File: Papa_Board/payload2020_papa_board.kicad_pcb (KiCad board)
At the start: 4 copper layers, 82 x 82 mm, 88 parts, among them J1 Conn_01x02_Female, J10 Conn_01x02_Female, J2 Conn_01x05, J3 Conn_01x05_Female, J4 Conn_01x05, J5 M80-5000642, J6 M80-5000642, J7 Conn_01x02_Female, J8 693072010801, J9 Conn_01x02_Female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

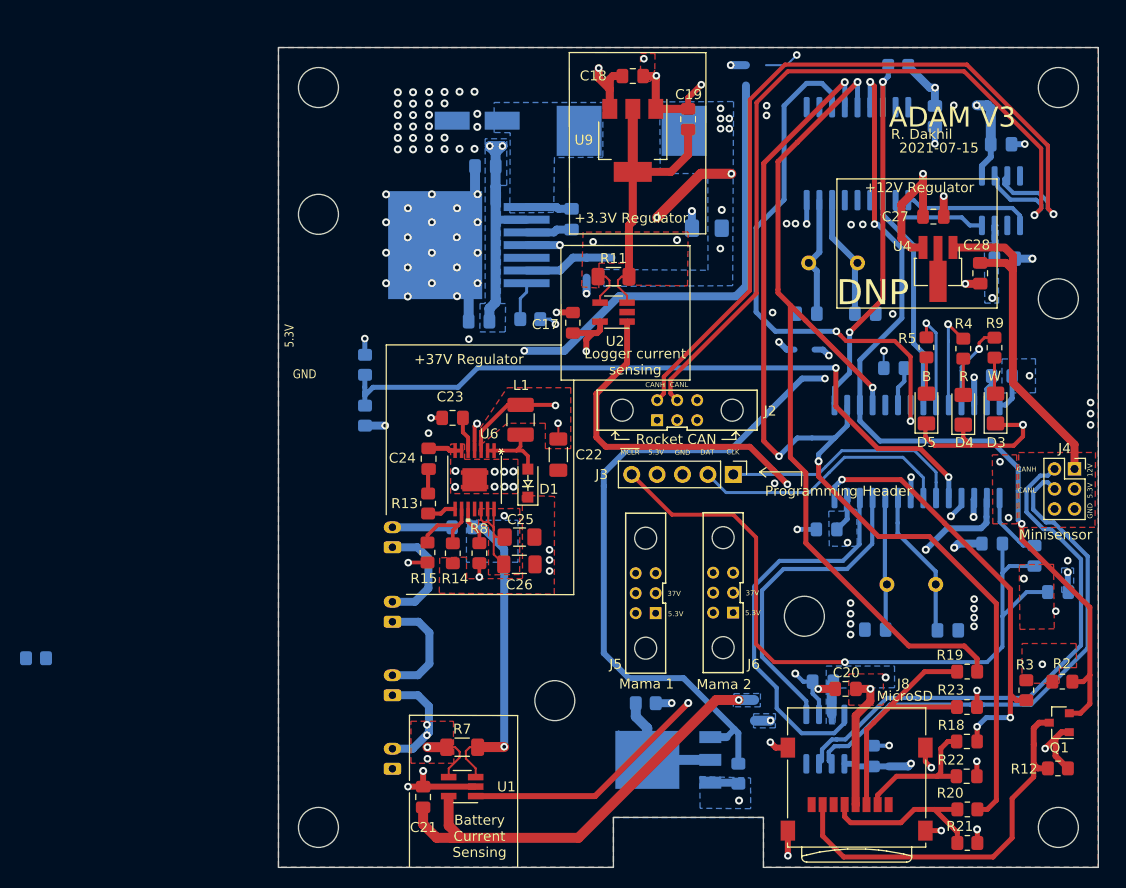
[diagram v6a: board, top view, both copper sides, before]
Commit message: Finish changes to PCB layout, clean up and simplify VCC layer
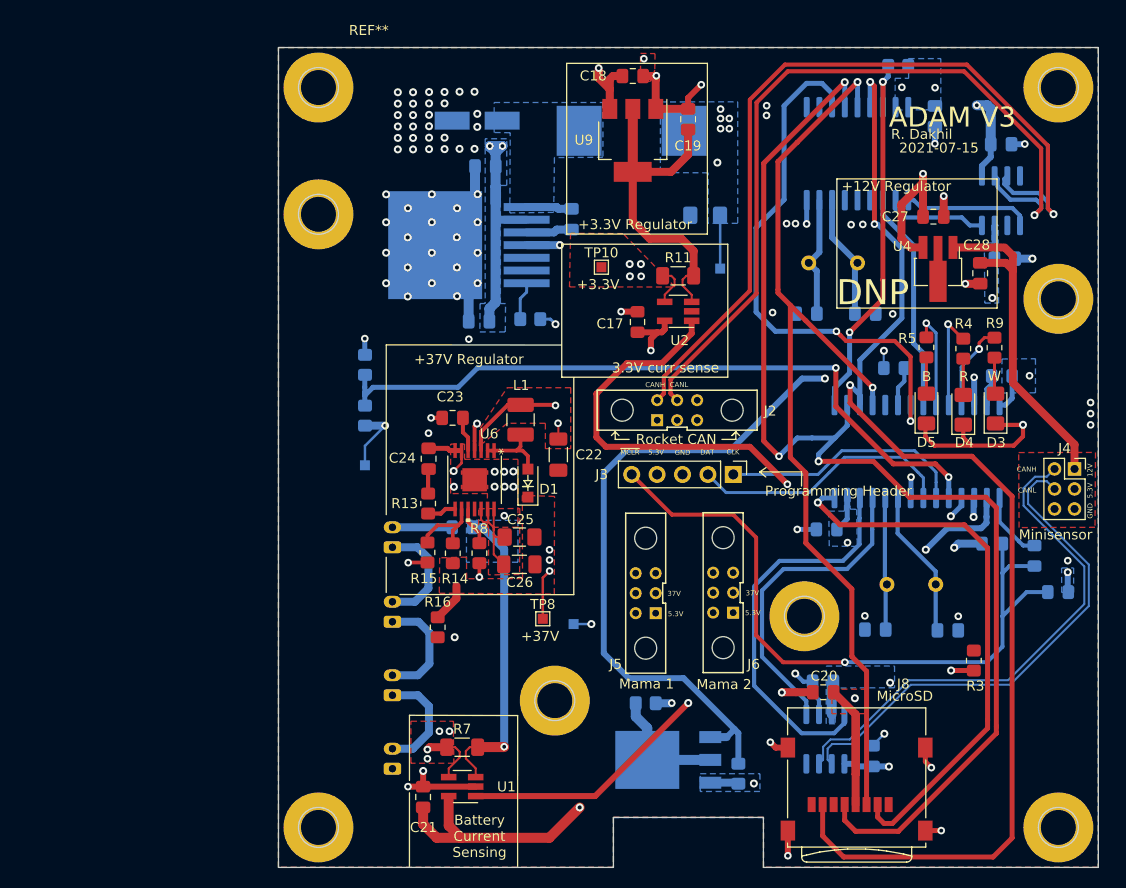
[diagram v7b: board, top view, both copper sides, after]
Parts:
- removed Q1: BSS138, Package_TO_SOT_SMD:SOT-23
- removed R12, R2: 10kR, Resistor_SMD:R_0805_2012Metric_Pad1.20x1.40mm_HandSolder
- removed R18: 68kR, Resistor_SMD:R_0805_2012Metric_Pad1.15x1.40mm_HandSolder
- removed R19, R20: 68kR, Resistor_SMD:R_0805_2012Metric_Pad1.20x1.40mm_HandSolder
- removed R21, R23: 132kR, Resistor_SMD:R_0805_2012Metric_Pad1.20x1.40mm_HandSolder
- removed R22: 132kR, Resistor_SMD:R_0805_2012Metric_Pad1.15x1.40mm_HandSolder
- added ?: , , F.Cu at (93.1, 83.8)
- added ?: , , F.Cu at (92.2, 149.0)
- added ?: , , F.Cu at (189.9, 144.5)
- added ?: , , F.Cu at (192.2, 123.9)
- added ?: , , F.Cu at (129.5, 133.1)
- added ?: , , F.Cu at (190.0, 70.3)
- added ?: , , F.Cu at (191.4, 93.3)
- added REF**: MountingHole_3.5mm_Pad, MountingHole:MountingHole_3.5mm_Pad, F.Cu at (110.9, 70.6)
- added TP10: TestPoint, TestPoint:TestPoint_Pad_1.0x1.0mm, F.Cu at (134.2, 89.8)
- added TP2: TestPoint, TestPoint:TestPoint_Pad_1.0x1.0mm, B.Cu at (131.4, 125.5)
- added TP3: TestPoint, TestPoint:TestPoint_Pad_1.0x1.0mm, B.Cu at (110.5, 109.6)
- added TP6: TestPoint, TestPoint:TestPoint_Pad_1.0x1.0mm, B.Cu at (146.0, 89.9)
- added TP8: TestPoint, TestPoint:TestPoint_Pad_1.0x1.0mm, F.Cu at (128.3, 125.0)
- R16: moved to F.Cu
- moved R16 40.3 mm to (117.8, 125.8), turned to -90 degrees
- moved C17 6.47 mm to (137.8, 95.3)
- moved R11 6.47 mm to (141.8, 90.6)
- moved U2 6.47 mm to (141.8, 94.2)
- moved R3 6.03 mm to (171.4, 129.1), turned to 90 degrees
- moved C20 2.25 mm to (156.3, 132.3)
- moved C7 1.30 mm to (144.5, 84.6)
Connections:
- net /+ renamed /CANH_PAYLOAD
- net /- renamed /CANL_PAYLOAD
- C21 pad 2: +5.3V -> +5V
- C25 pad 1: Net-(C25-Pad1) -> +37V
- C26 pad 1: Net-(C25-Pad1) -> +37V
- D1 pad 1: Net-(C25-Pad1) -> +37V
- J5 pad 2: Net-(J5-Pad2) -> +37V
- J6 pad 2: Net-(J6-Pad2) -> +37V
- J8 pad 2: Net-(J8-Pad2) -> /MCU and CAN controllers/CS_2
- J8 pad 3: Net-(J8-Pad3) -> /MCU and CAN controllers/MOSI
- J8 pad 5: Net-(J8-Pad5) -> /MCU and CAN controllers/SCK
- J8 pad 7: Net-(J8-Pad7) -> /MCU and CAN controllers/MISO
- R14 pad 1: Net-(C25-Pad1) -> +37V
- R16 pad 1: Net-(C25-Pad1) -> +37V
- U1 pad 5: +5.3V -> +5V
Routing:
- net +5.3V: track 47.1 -> 0.00 mm, vias 3 -> 0
- net Net-(J8-Pad7): track 39.0 -> 0.00 mm
- net /MCU and CAN controllers/MISO: track 88.5 -> 120.3 mm
- net +3V3: track 67.8 -> 36.7 mm, vias 11 -> 8
- net Net-(J8-Pad3): track 26.0 -> 0.00 mm
- net Net-(J8-Pad5): track 17.6 -> 0.00 mm
- net /MCU and CAN controllers/SCK: track 104.1 -> 120.6 mm
- net Net-(J8-Pad2): track 14.4 -> 0.00 mm
- net /MCU and CAN controllers/CS_2: track 43.5 -> 55.2 mm, vias 3 -> 1
- net unconnected-(U3-Pad6): track 9.09 -> 0.00 mm
- net +37V: track 0.00 -> 8.99 mm, vias 0 -> 3
- net +5V: track 136.0 -> 142.0 mm, vias 19 -> 17
- net /MCU and CAN controllers/MOSI: track 89.8 -> 95.1 mm
- net (no net): track 5.07 -> 0.00 mm, vias 2 -> 0
- net 3V3_CURR_AMP: track 56.4 -> 61.2 mm
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- added copper zone on F.Cu, net +37V
- added copper zone on In2.Cu, net +37V
- removed copper zone on F.Cu, net +5.3V
- removed copper zone on F.Cu, net Net-(C25-Pad1)
- removed copper zone on In2.Cu, net Net-(J5-Pad2)
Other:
- board text added: "+3.3V"
- board text added: "+37V"
- board text added: "+5V"
- board text added: "+5V Regulator"
- board text added: "+5V_MAMA"
- board text added: "+BATT"
- board text added: "3.3V curr sense"
- board text removed: "+5.3V ALWAYS ON"
- board text removed: "+5.3V Regulator"
- board text removed: "Logger current sensing"

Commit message: Connect TPS61175 NC pin to GND and update date on silkscreen
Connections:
- U6 pad 11: unconnected-(U6-Pad11) -> GND
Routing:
- net GND: track 113.7 -> 116.2 mm
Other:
- board text added: "2022-05-12"
- board text removed: "2021-07-15"
